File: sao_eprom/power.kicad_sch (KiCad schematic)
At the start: 7 parts, among them U9 AP3012

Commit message: I know how 2 power now
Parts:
- added C12, C13, C14, C15: 1uF, Capacitor_THT:C_Disc_D3.0mm_W1.6mm_P2.50mm, symbol Device:C
- added D4, D5: 1N5819, Diode_THT:D_DO-41_SOD81_P10.16mm_Horizontal, symbol Diode:1N5819
- added L2, L3: 10uH, Inductor_SMD:L_0805_2012Metric, symbol Device:L
- added R6, R7, R8, R9: R, Resistor_THT:R_Axial_DIN0207_L6.3mm_D2.5mm_P7.62mm_Horizontal, symbol Device:R
- added U10, U9: AP3012, Package_TO_SOT_SMD:SOT-23-5, symbol Regulator_Switching:AP3012
- renumbered U9 to U8
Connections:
- net +3V3: now also C12.2, C14.2, L2.1, L3.1, U10.4 (~{SHDN}), U10.5 (IN), U9.4 (~{SHDN})
- net 12V5EN: now also U8.5 (IN)
- net 6V25: now also C13.2, D4.1 (K), R6.1
- net 6V25EN: now also U9.5 (IN)
- net GND: now also C12.1, C13.1, C14.1, C15.1, R7.2, R9.2, U10.2 (GND), U9.2 (GND)
- new net: R6.2, R7.1, U9.3 (FB)
- new net: D5.2 (A), L3.2, U10.1 (SW)
- new net: R8.2, R9.1, U10.3 (FB)
- new net: D4.2 (A), L2.2, U9.1 (SW)
- new net 5V: C15.2, D5.1 (K), R8.1
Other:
- note added: "Target voltage = 5V Vout = 1.25*(1+R4/R5) R4/R5 = 3"
- note added: "Target voltage = 6.25V Vout = 1.25*(1+R4/R5) R4/R5 = 4"

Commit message: asdafdafa
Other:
- note added: "Target voltage = 12.75V Vout = 1.25*(1+R4/R5) R4/R5 = 9.2"
- note removed: "Target voltage = 12.5V Vout = 1.25*(1+R4/R5) R4/R5 = 9"
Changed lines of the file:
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@@
     (stroke (width 0) (type default) (color 0 0 0 0))
   )
-  (text "Target voltage	= 12.5V\nVout			= 1.25*(1+R4/R5)\nR4/R5			= 9"
+  (text "Target voltage	= 12.75V\nVout			= 1.25*(1+R4/R5)\nR4/R5			= 9.2"
     (at 22.86 54.61 0)
     (effects (font (size 1.27 1.27)) (justify left bottom))

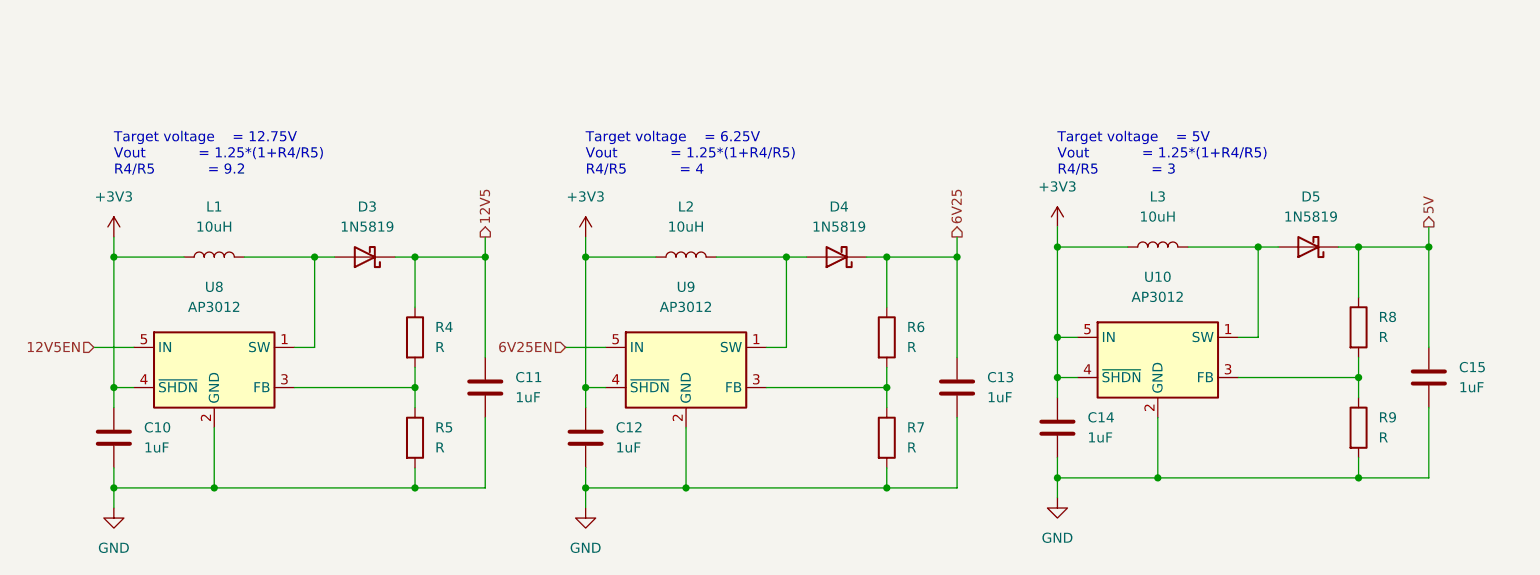
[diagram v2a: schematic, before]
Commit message: Do some resistor calculations
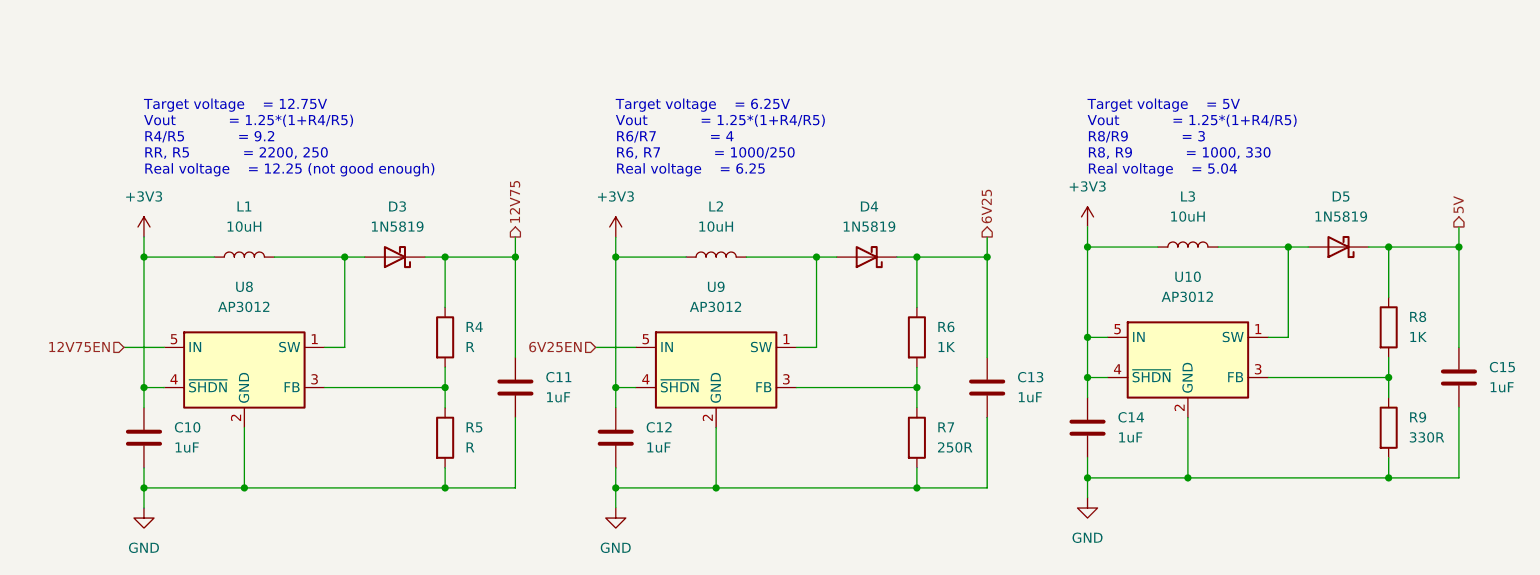
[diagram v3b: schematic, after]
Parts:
- R6, R8: value R -> 1K
- R7: value R -> 250R
- R9: value R -> 330R
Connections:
- net 12V5 renamed 12V75
- net 12V5EN renamed 12V75EN
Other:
- note added: "Target voltage = 12.75V Vout = 1.25*(1+R4/R5) R4/R5 = 9.2 RR, R5 = 2200, 250 Real voltage = 12.25 (not good enough)"
- note added: "Target voltage = 5V Vout = 1.25*(1+R4/R5) R8/R9 = 3 R8, R9 = 1000, 330 Real voltage = 5.04"
- note added: "Target voltage = 6.25V Vout = 1.25*(1+R4/R5) R6/R7 = 4 R6, R7 = 1000/250 Real voltage = 6.25"
- note removed: "Target voltage = 12.75V Vout = 1.25*(1+R4/R5) R4/R5 = 9.2"
- note removed: "Target voltage = 5V Vout = 1.25*(1+R4/R5) R4/R5 = 3"
- note removed: "Target voltage = 6.25V Vout = 1.25*(1+R4/R5) R4/R5 = 4"
- title: (none) -> Power generation
- moved on the sheet: C10, C11, C12, C13, C14, C15, D3, D4, D5, L1, L2, L3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

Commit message: Choose final resistor values
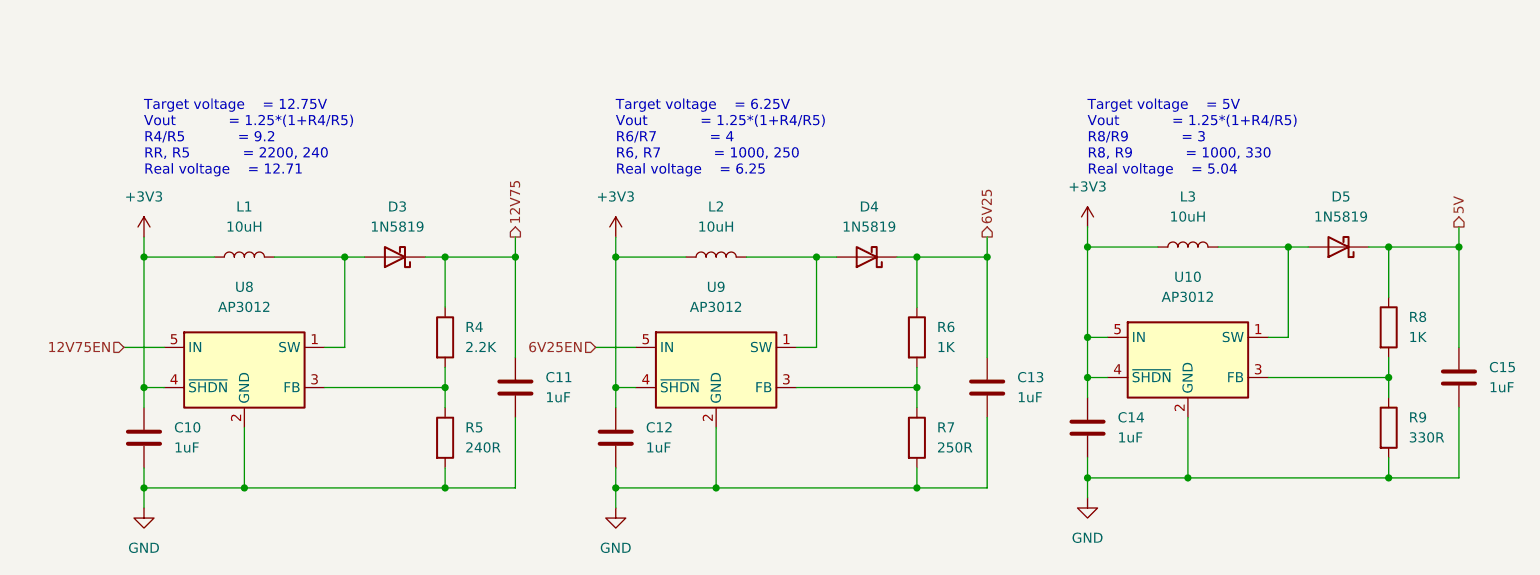
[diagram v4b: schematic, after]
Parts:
- R4: value R -> 2.2K
- R5: value R -> 240R
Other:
- note added: "Target voltage = 12.75V Vout = 1.25*(1+R4/R5) R4/R5 = 9.2 RR, R5 = 2200, 240 Real voltage = 12.71"
- note added: "Target voltage = 6.25V Vout = 1.25*(1+R4/R5) R6/R7 = 4 R6, R7 = 1000, 250 Real voltage = 6.25"
- note removed: "Target voltage = 12.75V Vout = 1.25*(1+R4/R5) R4/R5 = 9.2 RR, R5 = 2200, 250 Real voltage = 12.25 (not good enough)"
- note removed: "Target voltage = 6.25V Vout = 1.25*(1+R4/R5) R6/R7 = 4 R6, R7 = 1000/250 Real voltage = 6.25"
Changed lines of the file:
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@@
     (stroke (width 0) (type default) (color 0 0 0 0))
   )
-  (text "Target voltage	= 12.75V\nVout			= 1.25*(1+R4/R5)\nR4/R5			= 9.2\nRR, R5			= 2200, 250\nReal voltage	= 12.25 (not good enough)"
+  (text "Target voltage	= 12.75V\nVout			= 1.25*(1+R4/R5)\nR4/R5			= 9.2\nRR, R5			= 2200, 240\nReal voltage	= 12.71"
     (at 26.67 54.61 0)
     (effects (font (size 1.27 1.27)) (justify left bottom))
   )
-  (text "Target voltage	= 6.25V\nVout			= 1.25*(1+R4/R5)\nR6/R7			= 4\nR6, R7			= 1000/250\nReal voltage	= 6.25"
+  (text "Target voltage	= 6.25V\nVout			= 1.25*(1+R4/R5)\nR6/R7			= 4\nR6, R7			= 1000, 250\nReal voltage	= 6.25"
     (at 86.36 54.61 0)
     (effects (font (size 1.27 1.27)) (justify left bottom))
@@
       (effects (font (size 1.27 1.27)) (justify left))
     )
-    (property "Value" "R" (id 1) (at 67.31 88.8999 0)
+    (property "Value" "240R" (id 1) (at 67.31 88.8999 0)
       (effects (font (size 1.27 1.27)) (justify left))
     )
@@
       (effects (font (size 1.27 1.27)) (justify left))
     )
-    (property "Value" "R" (id 1) (at 67.31 76.1999 0)
-      (effects (font (size 1.27 1.27)) (justify left))
-    )
+    (property "Value" "2.2K" (id 1) (at 67.31 76.1999 0)
+      (effects (font (size 1.27 1.27)) (justify left))
+    )
